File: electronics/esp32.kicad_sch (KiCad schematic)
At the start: 39 parts, among them J2 Conn_02x03_Odd_Even, J3 Conn_01x03, SW1 SW_Push, SW2 SW_Push, U5 ESP32-S3-WROOM-1, U6 W25Q16JVSS, Y1 FC-135_32.7680KA-A0

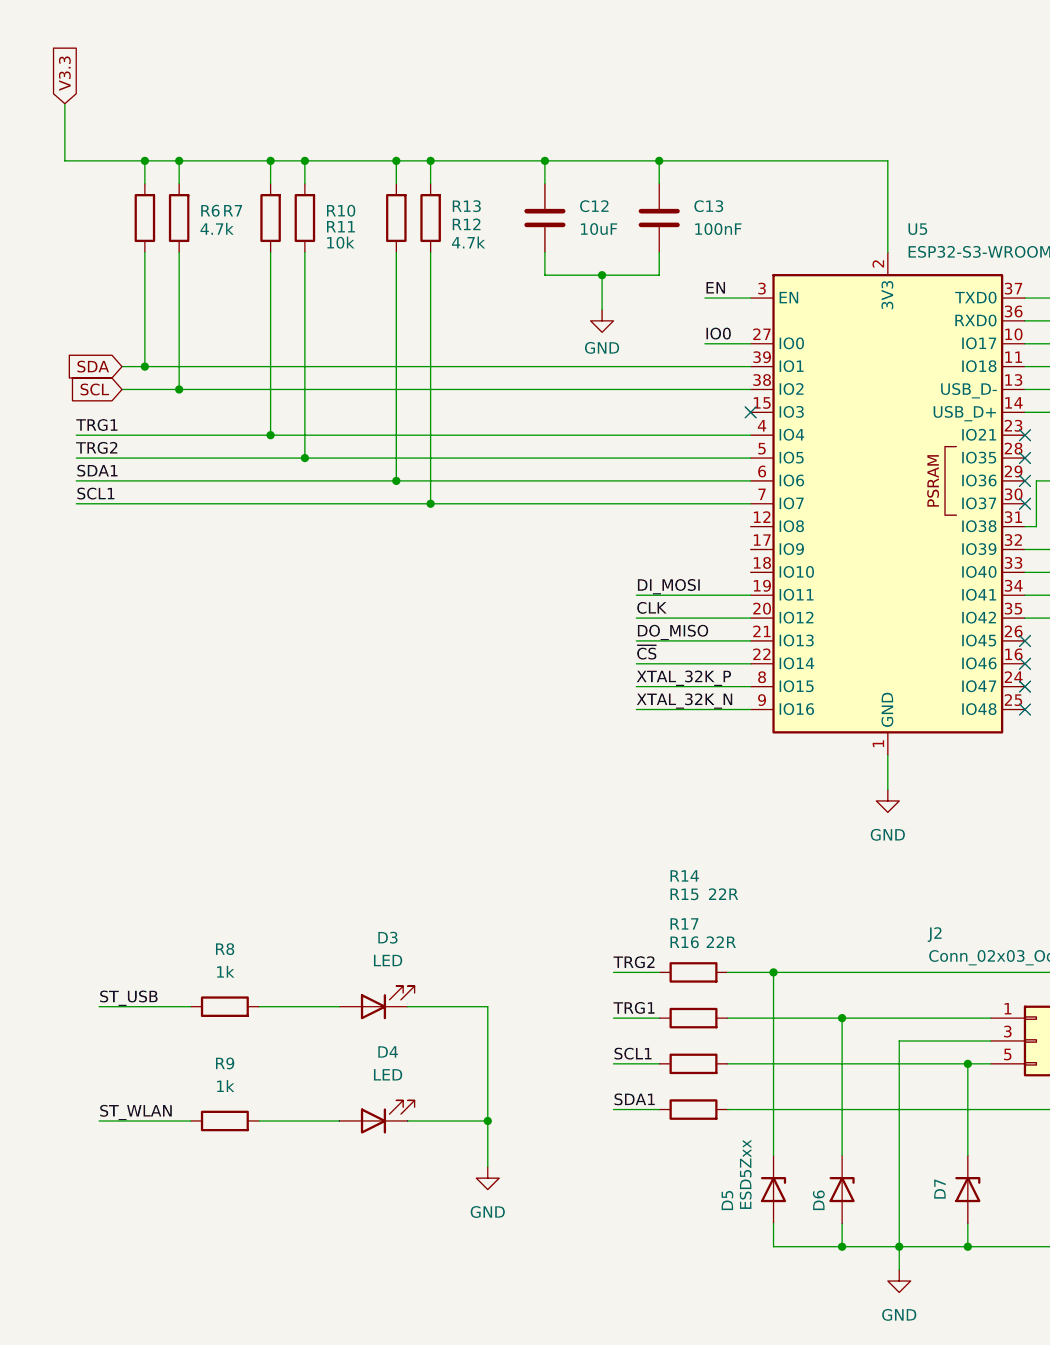
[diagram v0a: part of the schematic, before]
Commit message: Added IO3 pullup and negative 3V3 rail testpoint, few other PCB layput improvements.
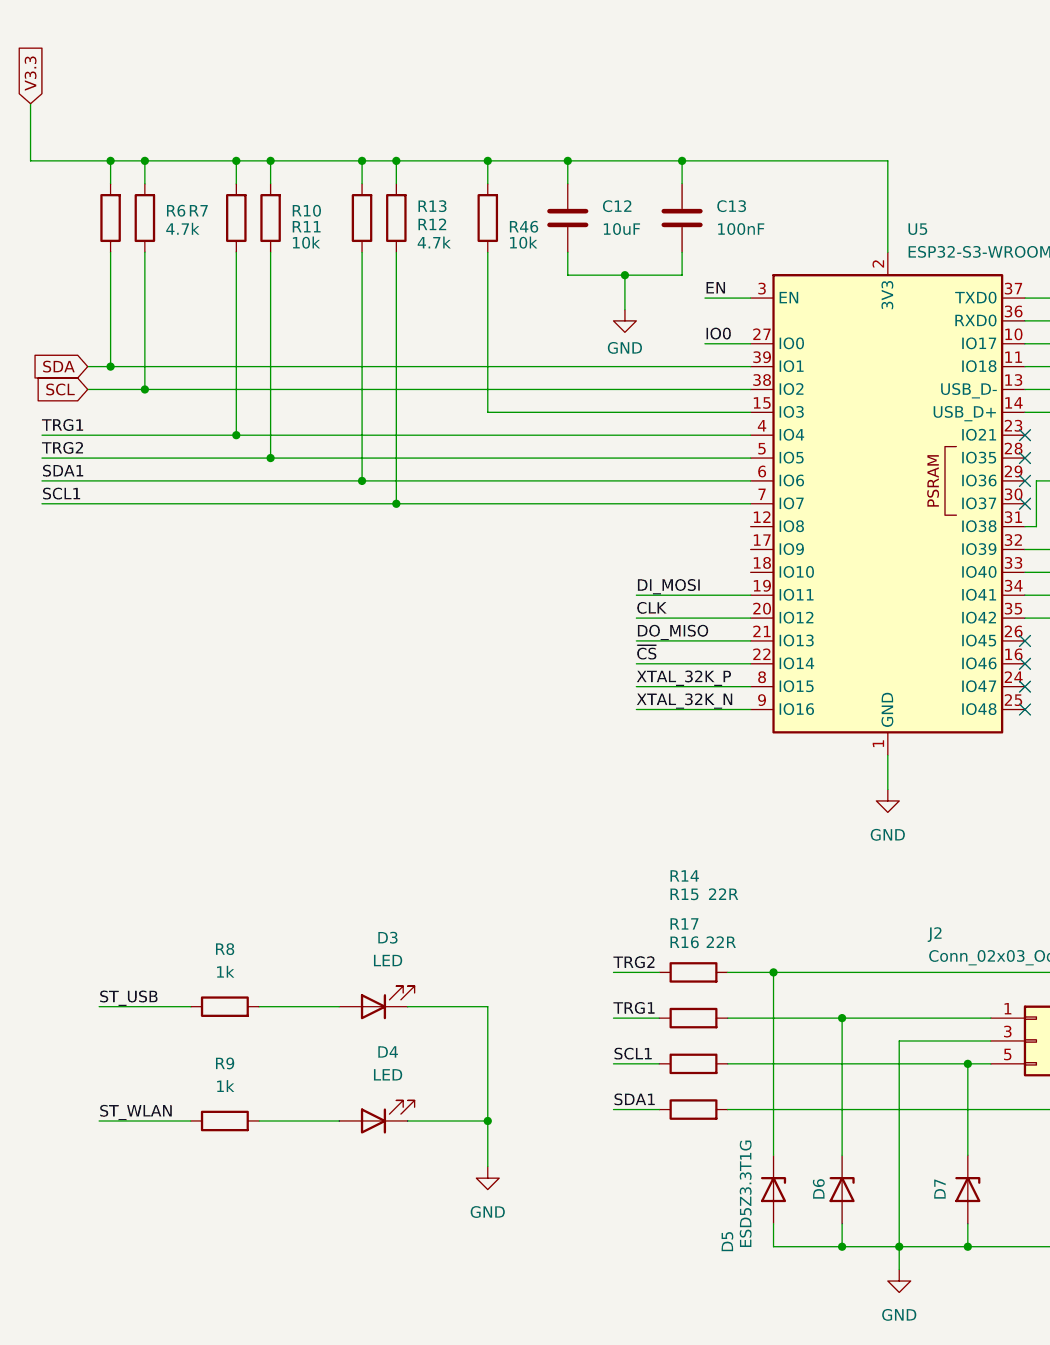
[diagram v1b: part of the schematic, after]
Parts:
- added R46: 10k, Resistor_SMD:R_0805_2012Metric, symbol Device:R
- D6, D7, D8, D9: value ESD5Zxx -> ESD5Z3.3T1G
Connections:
- net V3.3: now also R46.2
- net at U5.15 (IO3): now also R46.1
- no-connect marks 9 -> 8
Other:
- moved on the sheet: C12, C13, R10, R11, R12, R13, R6, R7

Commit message: Fixex for proect before PCBA. TODO. BOM, CPL, EXPORT
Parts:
- D5: value ESD5Zxx -> ESD5Z3.3T1G
- D9: now left out of the parts list
- R22: renamed from R21; now not fitted; now left out of the parts list
- R23: renamed from R22; now not fitted; now left out of the parts list
- renumbered R46 to R14, R14 to R15, R15 to R16, R16 to R17, R17 to R18, R18 to R19, R19 to R20, R20 to R21
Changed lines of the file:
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@@
 		(in_pos_files yes)
 		(dnp no)
-		(property "Reference" "R15"
+		(property "Reference" "R16"
 			(at 90.424 114.554 90)
 			(show_name no)
@@
 			(project "psu-ext"
 				(path "/3cca1064-5b2a-48a0-8872-f4d00db38e9c/b81da866-3687-4f09-9daf-01c24fc18b36"
-					(reference "R15")
+					(reference "R16")
 					(unit 1)
 				)
@@
 		)
 		(property "Value" "ESD5Z3.3T1G"
-			(at 97.282 141.732 0)
+			(at 101.346 156.972 0)
+			(hide yes)
 			(show_name no)
 			(do_not_autoplace no)
@@
 		(in_pos_files yes)
 		(dnp no)
-		(property "Reference" "R17"
+		(property "Reference" "R18"
 			(at 90.424 117.856 90)
 			(show_name no)
@@
 			(project "psu-ext"
 				(path "/3cca1064-5b2a-48a0-8872-f4d00db38e9c/b81da866-3687-4f09-9daf-01c24fc18b36"
-					(reference "R17")
+					(reference "R18")
 					(unit 1)
 				)
@@
 		(body_style 1)
 		(exclude_from_sim no)
-		(in_bom yes)
+		(in_bom no)
 		(on_board yes)
-		(in_pos_files yes)
-		(dnp no)
-		(property "Reference" "R21"
+		(in_pos_files no)
+		(dnp yes)
+		(property "Reference" "R22"
 			(at 248.92 30.734 90)
 			(show_name no)
@@
 			(project "psu-ext"
 				(path "/3cca1064-5b2a-48a0-8872-f4d00db38e9c/b81da866-3687-4f09-9daf-01c24fc18b36"
-					(reference "R21")
+					(reference "R22")
 					(unit 1)
 				)
@@
 			)
 		)
-		(property "Value" "ESD5Zxx"
-			(at 102.87 148.5899 90)
-			(hide yes)
+		(property "Value" "ESD5Z3.3T1G"
+			(at 97.536 141.986 0)
 			(show_name no)
 			(do_not_autoplace no)
@@
 		(in_pos_files yes)
 		(dnp no)
-		(property "Reference" "R14"
+		(property "Reference" "R15"
 			(at 90.424 112.522 90)
 			(show_name no)
@@
 			(project "psu-ext"
 				(path "/3cca1064-5b2a-48a0-8872-f4d00db38e9c/b81da866-3687-4f09-9daf-01c24fc18b36"
-					(reference "R14")
+					(reference "R15")
 					(unit 1)
 				)
@@
 		(in_pos_files yes)
 		(dnp no)
-		(property "Reference" "R46"
+		(property "Reference" "R14"
 			(at 70.866 40.386 0)
 			(show_name no)
@@
 			(project "psu-ext"
 				(path "/3cca1064-5b2a-48a0-8872-f4d00db38e9c/b81da866-3687-4f09-9daf-01c24fc18b36"
-					(reference "R46")
+					(reference "R14")
 					(unit 1)
 				)
@@
 		(in_pos_files no)
 		(dnp yes)
-		(property "Reference" "R20"
+		(property "Reference" "R21"
 			(at 231.394 89.916 90)
 			(show_name no)
@@
 			(project "psu-ext"
 				(path "/3cca1064-5b2a-48a0-8872-f4d00db38e9c/b81da866-3687-4f09-9daf-01c24fc18b36"
-					(reference "R20")
+					(reference "R21")
 					(unit 1)
 				)
@@
 		(dnp no)
 		(fields_autoplaced yes)
-		(property "Reference" "R18"
+		(property "Reference" "R19"
 			(at 161.29 25.4 90)
 			(show_name no)
@@
 			(project "psu-ext"
 				(path "/3cca1064-5b2a-48a0-8872-f4d00db38e9c/b81da866-3687-4f09-9daf-01c24fc18b36"
-					(reference "R18")
+					(reference "R19")
 					(unit 1)
 				)
@@
 		(body_style 1)
 		(exclude_from_sim no)
-		(in_bom yes)
+		(in_bom no)
 		(on_board yes)
-		(in_pos_files yes)
-		(dnp no)
-		(property "Reference" "R22"
+		(in_pos_files no)
+		(dnp yes)
+		(property "Reference" "R23"
 			(at 248.92 37.846 90)
 			(show_name no)
@@
 			(project "psu-ext"
 				(path "/3cca1064-5b2a-48a0-8872-f4d00db38e9c/b81da866-3687-4f09-9daf-01c24fc18b36"
-					(reference "R22")
+					(reference "R23")
 					(unit 1)
 				)
@@
 		(in_pos_files yes)
 		(dnp no)
-		(property "Reference" "R16"
+		(property "Reference" "R17"
 			(at 90.424 119.888 90)
 			(show_name no)
@@
 			(project "psu-ext"
 				(path "/3cca1064-5b2a-48a0-8872-f4d00db38e9c/b81da866-3687-4f09-9daf-01c24fc18b36"
-					(reference "R16")
+					(reference "R17")
 					(unit 1)
 				)
@@
 		(in_pos_files no)
 		(dnp yes)
-		(property "Reference" "R19"
+		(property "Reference" "R20"
 			(at 224.282 89.916 90)
 			(show_name no)
@@
 			(project "psu-ext"
 				(path "/3cca1064-5b2a-48a0-8872-f4d00db38e9c/b81da866-3687-4f09-9daf-01c24fc18b36"
-					(reference "R19")
+					(reference "R20")
 					(unit 1)
 				)
@@
 		(body_style 1)
 		(exclude_from_sim no)
-		(in_bom yes)
+		(in_bom no)
 		(on_board yes)
-		(in_pos_files yes)
+		(in_pos_files no)
 		(dnp yes)
 		(property "Reference" "D9"
